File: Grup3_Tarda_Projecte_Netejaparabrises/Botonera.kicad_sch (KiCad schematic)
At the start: 0 parts

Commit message: canvis esquematic
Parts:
- added R3, R4, R5, R6: R, symbol Device:R
- added SW2, SW3, SW4, SW5: SW_Push, symbol Switch:SW_Push
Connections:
- new net +VCC: R3.1, R4.1, R5.1, R6.1
- new net GND: SW2.1, SW3.1, SW4.1, SW5.1
- new net Vb1: R3.2, SW2.2
- new net Vb2: R4.2, SW3.2
- new net Vb3: R5.2, SW4.2
- new net Vb4: R6.2, SW5.2
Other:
- note added: "BOTO 1"
- note added: "BOTO 2"
- note added: "BOTO 3"
- note added: "BOTO 4"
- note added: "BOTONERA"

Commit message: canvis esquematic
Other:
- title: (none) -> Projecte Netejaparabrises - Grup 4 Tarda
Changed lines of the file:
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@@
 (kicad_sch (version 20230121) (generator eeschema)
   (paper "A4")
+  (title_block
+    (title "Projecte Netejaparabrises - Grup 4 Tarda")
+    (date "2023-03-30")
+    (rev "v1.0.30032023")
+  )
   (junction (at 137.16 55.88) (diameter 0) (color 0 0 0 0)
   )

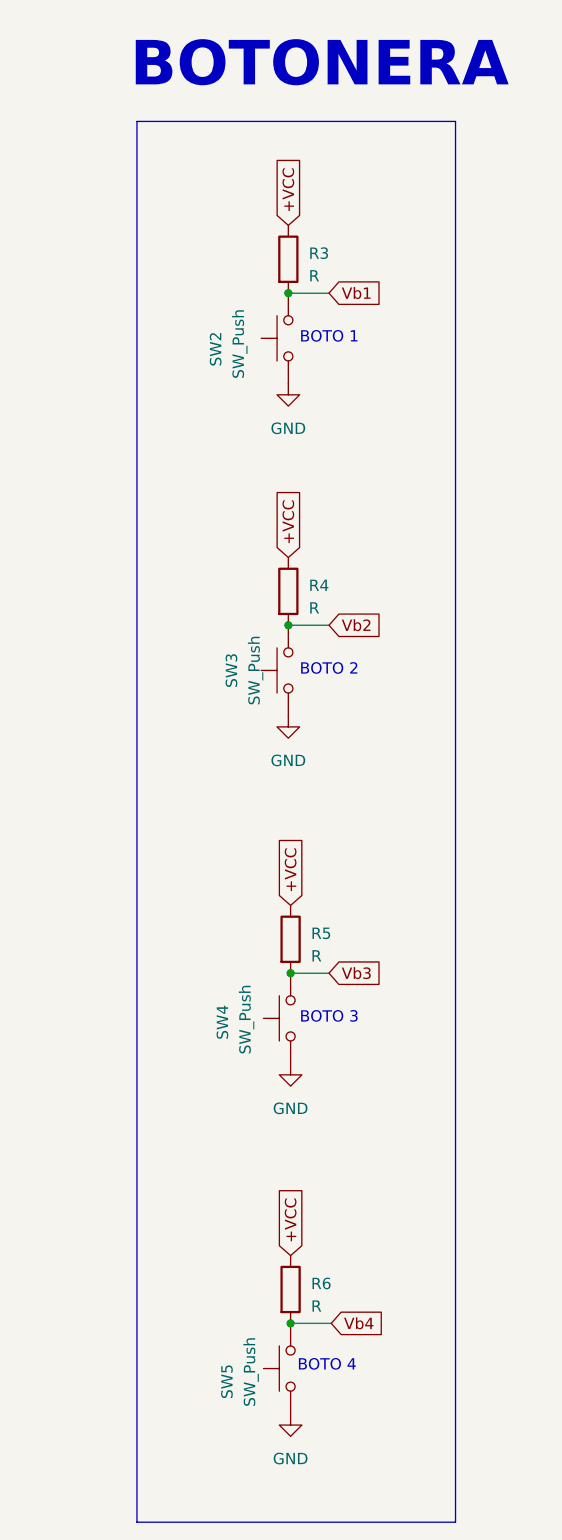
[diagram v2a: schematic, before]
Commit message: Modificat nets dels drivers de motors bombes... botonera i sensor de pluja millorats i amb connectors
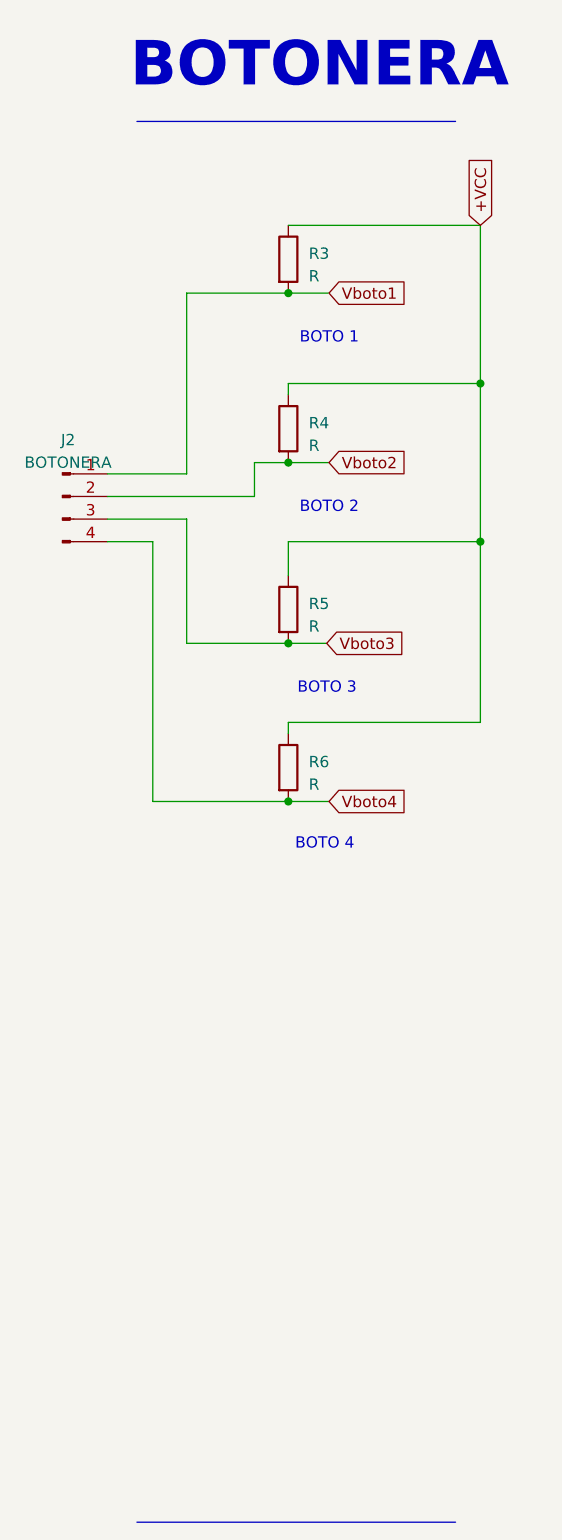
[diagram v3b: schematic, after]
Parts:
- removed SW2, SW3, SW4, SW5: SW_Push, symbol Switch:SW_Push
- added J2: BOTONERA, symbol Connector:Conn_01x04_Pin
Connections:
- net Vb1 renamed Vboto1
- net Vboto1: now also J2.1 (Pin_1)
- net Vb2 renamed Vboto2
- net Vboto2: now also J2.2 (Pin_2)
- net Vb3 renamed Vboto3
- net Vboto3: now also J2.3 (Pin_3)
- net Vb4 renamed Vboto4
- net Vboto4: now also J2.4 (Pin_4)
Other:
- moved on the sheet: R4, R5, R6
